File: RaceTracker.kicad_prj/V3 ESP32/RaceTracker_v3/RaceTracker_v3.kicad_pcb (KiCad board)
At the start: 2 copper layers, 50 x 73 mm, 39 parts, among them J1 USB-C, J2 Battery, J3 Qwiic GPS (I2C), J4 microSD, J5 UART Debug, SW1 PWR, SW2 RESET, SW3 BOOT, U1 ESP32-S3-WROOM-1-N8, U2 MCP73831T-2ACI/OT, U3 AP2112K-3.3

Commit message: V3: Wuerth WSEN-ISDS (2536030320001) 6-Achsen-IMU ergaenzt
Beschaltung exakt nach Datenblatt (Rev 001.005, 2025-10-30):
- VDD + VDD_IO an +3V3, je 100nF Entkopplung (C11/C12) -- Standard-
  Bypass-Praxis, da dieses Datenblatt (anders als ESP32/MCP73831/
  AP2112K) keine eigene Beispielschaltung zeigt.
- Pin 2/3 (RSVD) zwingend an VDD_IO (Datenblatt: "Optimize power
  consumption during device start-up sequence").
- Pin 11 (RSVD) an VDD_IO (Datenblatt bietet Wahl: VDD_IO oder NC).
- Pin 10 (RSVD) explizit unverbunden (Datenblatt: "Leave electrically
  unconnected and solder to the PCB").
- CS an VDD_IO (aktiviert I2C-Modus statt SPI).
- SAO ueber R15 (10k) nach GND (I2C-Adresse) -- Pull-Widerstand statt
  Direktverbindung, passend zum Board-Konvention (R1-R14 sind alle
  Pull-Widerstaende) und vermeidet eine ERC-Warnung (Bidirectional-Pin
  direkt an denselben Netz-Knoten wie der GND-PWR_FLAG).
- SCL/SDA an den bestehenden I2C-Bus (teilt sich mit dem externen
  GPS-Modul an J3).
- INT_0/INT_1 offen (optionale Wake/Data-Ready-Ausgaenge, fuer reines
  I2C-Polling nicht noetig) -- explizite No-Connect-Marker.

Kein offizielles KiCad-Symbol fuer dieses Bauteil vorhanden -- eigenes
14-Pin-Symbol gezeichnet, echtes Footprint "Package_LGA:LGA-14_3x2.5mm_
P0.5mm_LayoutBorder3x4y" (urspruenglich fuer ST LSM6DS3 erstellt --
identisches LGA-14/0.5mm-Pitch/3-4-3-4-Pinout-Package, Land-Pattern-Maße
im WSEN-ISDS-Datenblatt gegengeprueft). Neue projektlokale Symbolbib-
liothek RaceTracker_v3.kicad_sym + sym-lib-table angelegt (vermeidet
die lib_symbol_issues-Warnung).

Platine von 50x73mm auf 50x85mm vergroessert (war bereits komplett
vollgepackt, kein Platz fuer 4 neue Bauteile) -- neue Reihe U4/R15/C11/
C12 unten platziert, bestehende Platzierung unangetastet. Default-
Clearance von 0.2mm auf 0.127mm gelockert (die LGA-14-eigenen Pads
liegen bauartbedingt bei 0.5mm Pitch teils nur 0.15-0.175mm auseinander
-- selbe Art Fix wie zuvor bei den ESP32-EPAD-Vias).

ERC: 0 Fehler, 0 Warn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
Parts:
- added C11: 100nF, C_0603_1608Metric, F.Cu at (28.0, 79.0)
- added C12: 100nF, C_0603_1608Metric, F.Cu at (36.0, 79.0)
- added R15: 10k, R_0603_1608Metric, F.Cu at (20.0, 79.0)
- added U4: WSEN-ISDS, LGA-14_3x2.5mm_P0.5mm_LayoutBorder3x4y, F.Cu at (10.0, 79.0)
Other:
- board size 50 x 73 mm -> 50 x 85 mm

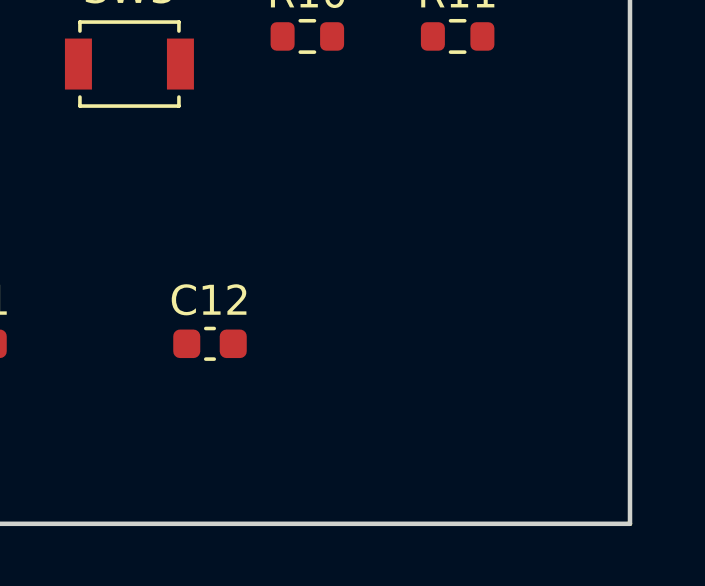
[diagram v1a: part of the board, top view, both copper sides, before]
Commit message: V3: PCB auf 4 Lagen (JLCPCB-Standard-Stackup) + C13 (10uF) fuer WSEN-ISDS
Layer-Stackup 2 -> 4 Lagen (In1.Cu/In2.Cu ergaenzt), physischer Aufbau
exakt nach JLCPCB-Standard-4-Lagen-1.6mm-Build (JLC7628-Klasse):
F.Cu 1oz / Prepreg 7628 0.2104mm / In1.Cu 0.5oz / Core FR4 1.065mm /
In2.Cu 0.5oz / Prepreg 7628 0.2104mm / B.Cu 1oz -- angelegt fuer GND-
und VCC-Plane auf den Innenlagen (Zonen/Pours folgen beim eigentlichen
Routing).

C13 (10uF, 0805) ergaenzt: erneute Pruefung von Wuerths eigenem
"Application circuit" (User Manual Figur 3, Seite 17) zeigte, dass VDD
zusaetzlich zum 100nF (C11) auch einen 10uF-Bulk-Kondensator parallel
braucht ("highly recommended") -- war in der ersten Bestueckung uebersehen
worden. VDD_IO (C12, nur 100nF) stimmte bereits exakt mit der Abbildung
ueberein. User-Manual als Referenz mit im Projekt abgelegt.

ERC: 0/0. DRC: 0 Violations, 122 unverbundene Punkte (weiterhin
ungeroutet, erwartet).

Co-Authored-By: Claude Sonnet 5 <noreply@anthropic.com>
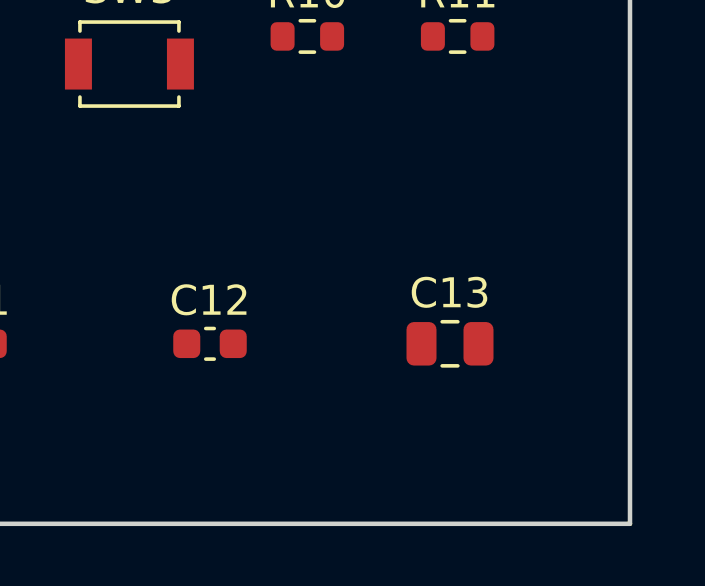
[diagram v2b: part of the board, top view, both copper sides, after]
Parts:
- added C13: 10uF, C_0805_2012Metric, F.Cu at (44.0, 79.0)
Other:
- copper layers 2 -> 4
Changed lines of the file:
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@@
 	(layers
 		(0 "F.Cu" signal)
+		(4 "In1.Cu" signal)
+		(6 "In2.Cu" signal)
 		(2 "B.Cu" signal)
 		(9 "F.Adhes" user "F.Adhesive")
@@
 	)
 	(setup
+		(stackup
+			(layer "F.SilkS"
+				(type "Top Silk Screen")
+			)
+			(layer "F.Paste"
+				(type "Top Solder Paste")
+			)
+			(layer "F.Mask"
+				(type "Top Solder Mask")
+				(thickness 0.01)
+			)
+			(layer "F.Cu"
+				(type "copper")
+				(thickness 0.035)
+			)
+			(layer "dielectric 1"
+				(type "prepreg")
+				(thickness 0.2104)
+				(material "PP 7628")
+				(epsilon_r 4.5)
+				(loss_tangent 0.02)
+			)
+			(layer "In1.Cu"
+				(type "copper")
+				(thickness 0.0175)
+			)
+			(layer "dielectric 2"
+				(type "core")
+				(thickness 1.065)
+				(material "FR4")
+				(epsilon_r 4.5)
+				(loss_tangent 0.02)
+			)
+			(layer "In2.Cu"
+				(type "copper")
+				(thickness 0.0175)
+			)
+			(layer "dielectric 3"
+				(type "prepreg")
+				(thickness 0.2104)
+				(material "PP 7628")
+				(epsilon_r 4.5)
+				(loss_tangent 0.02)
+			)
+			(layer "B.Cu"
+				(type "copper")
+				(thickness 0.035)
+			)
+			(layer "B.Mask"
+				(type "Bottom Solder Mask")
+				(thickness 0.01)
+			)
+			(layer "B.Paste"
+				(type "Bottom Solder Paste")
+			)
+			(layer "B.SilkS"
+				(type "Bottom Silk Screen")
+			)
+			(copper_finish "None")
+			(dielectric_constraints no)
+		)
 		(pad_to_mask_clearance 0)
 		(allow_soldermask_bridges_in_footprints no)
@@
 			(offset
 				(xyz 0 0 0)
+			)
+			(scale
+				(xyz 1 1 1)
+			)
+			(rotate
+				(xyz 0 0 0)
+			)
+		)
+	)
+	(footprint "C_0805_2012Metric"
+		(layer "F.Cu")
+		(at 44 79)
+		(descr "Capacitor SMD 0805 (2012 Metric), square (rectangular) end terminal, IPC-7351 nominal, (Body size source: IPC-SM-782 page 76, https://www.pcb-3d.com/wordpress/wp-content/uploads/ipc-sm-782a_amendment_1_and_2.pdf, https://docs.google.com/spreadsheets/d/1BsfQQcO9C6DZCsRaXUlFlo91Tg2WpOkGARC1WS5S8t0/edit?usp=sharing)")
+		(tags "capacitor")
+		(property "Reference" "C13"
+			(at 0 -1.68 0)
+			(layer "F.SilkS")
+			(effects
+				(font
+					(size 1 1)
+					(thickness 0.15)
+				)
+			)
+		)
+		(property "Value" "10uF"
+			(at 0 1.68 0)
+			(layer "F.Fab")
+			(effects
+				(font
+					(size 1 1)
+					(thickness 0.15)
+				)
+			)
+		)
+		(property "Datasheet" ""
+			(at 0 0 0)
+			(layer "F.Fab")
+			(hide yes)
+			(effects
+				(font
+					(size 1.27 1.27)
+				)
+			)
+		)
+		(property "Description" ""
+			(at 0 0 0)
+			(layer "F.Fab")
+			(hide yes)
+			(effects
+				(font
+					(size 1.27 1.27)
+				)
+			)
+		)
+		(property "KiLib_Generator" "SMD_2terminal_chip_molded"
+			(at 0 0 0)
+			(layer "F.SilkS")
+			(hide yes)
+			(effects
+				(font
+					(size 1 1)
+					(thickness 0.15)
+				)
+			)
+		)
+		(attr smd)
+		(duplicate_pad_numbers_are_jumpers no)
+		(fp_line
+			(start -0.261252 -0.735)
+			(end 0.261252 -0.735)
+			(stroke
+				(width 0.12)
+				(type solid)
+			)
+			(layer "F.SilkS")
+		)
+		(fp_line
+			(start -0.261252 0.735)
+			(end 0.261252 0.735)
+			(stroke
+				(width 0.12)
+				(type solid)
+			)
+			(layer "F.SilkS")
+		)
+		(fp_rect
+			(start -1.7 -0.98)
+			(end 1.7 0.98)
+			(stroke
+				(width 0.05)
+				(type solid)
+			)
+			(fill no)
+			(layer "F.CrtYd")
+		)
+		(fp_rect
+			(start -1 -0.625)
+			(end 1 0.625)
+			(stroke
+				(width 0.1)
+				(type solid)
+			)
+			(fill no)
+			(layer "F.Fab")
+		)
+		(fp_text user "${REFERENCE}"
+			(at 0 0 0)
+			(layer "F.Fab")
+			(effects
+				(font
+					(size 0.5 0.5)
+					(thickness 0.08)
+				)
+			)
+		)
+		(pad "1" smd roundrect
+			(at -0.95 0)
+			(size 1 1.45)
+			(layers "F.Cu" "F.Mask" "F.Paste")
+			(roundrect_rratio 0.25)
+			(net "/+3V3")
+		)
+		(pad "2" smd roundrect
+			(at 0.95 0)
+			(size 1 1.45)
+			(layers "F.Cu" "F.Mask" "F.Paste")
+			(roundrect_rratio 0.25)
+			(net "/GND")
+		)
+		(embedded_fonts no)
+		(model "${KICAD10_3DMODEL_DIR}/Capacitor_SMD.3dshapes/C_0805_2012Metric.step"
+			(offset
+				(xyz 0 0 0)

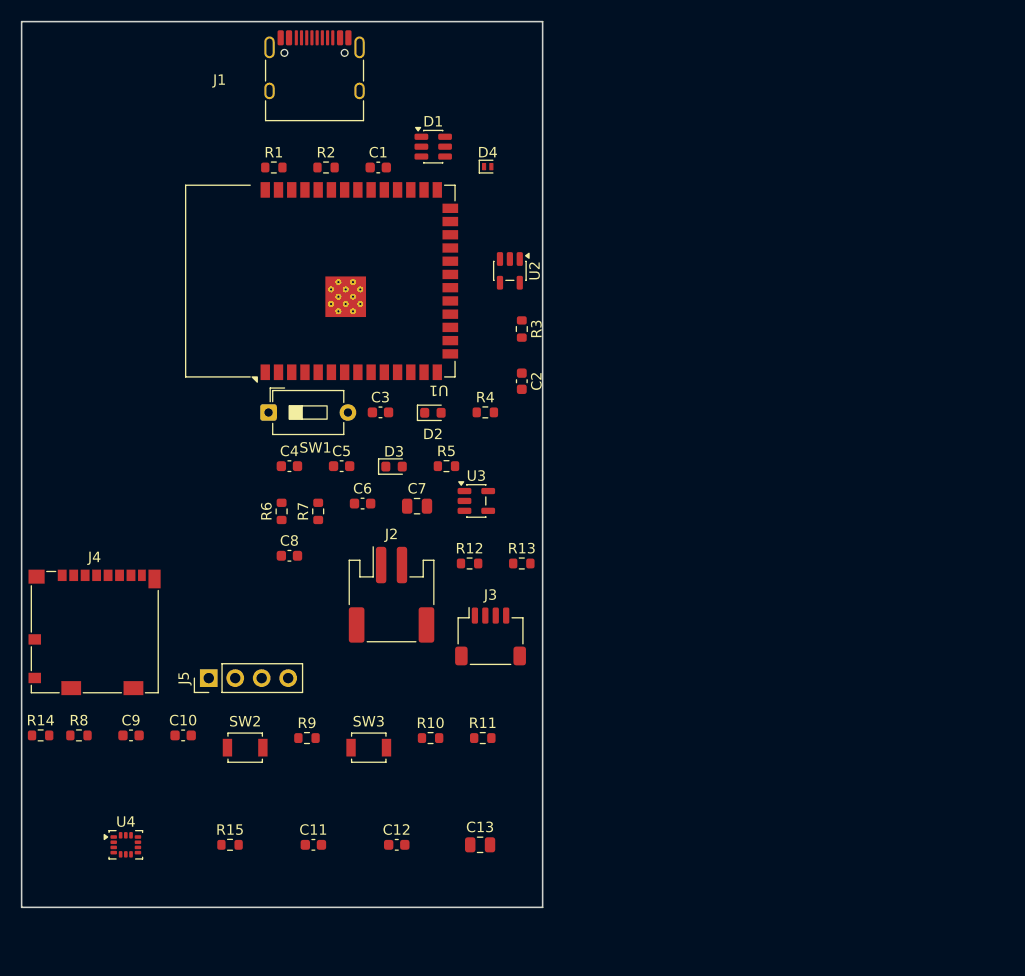
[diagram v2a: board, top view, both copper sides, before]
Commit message: V3: Board auf 50x87mm vergroessert, J6 am Rand platziert
Co-Authored-By: Claude Sonnet 5 <noreply@anthropic.com>
Claude-Session: https://claude.ai/code/session_01KJ1x8W8LsYuDo52VfB14br
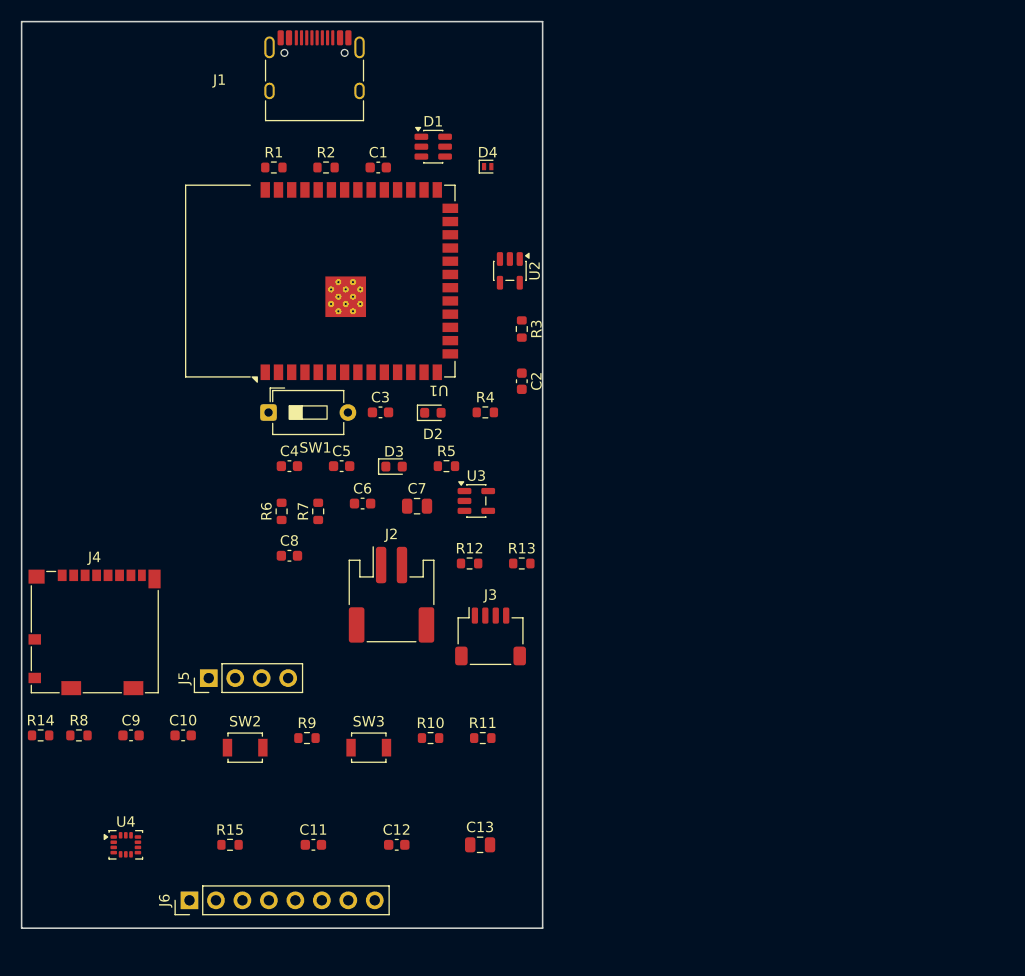
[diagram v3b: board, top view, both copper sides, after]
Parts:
- added J6: e-Paper (steckbar) 8p, PinHeader_1x08_P2.54mm_Vertical, F.Cu at (16.1, 84.3)
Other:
- board size 50 x 85 mm -> 50 x 87 mm

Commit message: V3: GND/+3V3 Planes, Power-Routing, Teilrouting der Signalnetze
Co-Authored-By: Claude Sonnet 5 <noreply@anthropic.com>
Claude-Session: https://claude.ai/code/session_01KJ1x8W8LsYuDo52VfB14br
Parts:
- moved U4 86.9 mm to (82.5, 31.0)
- moved J4 79.7 mm to (83.0, 82.5), turned to 90 degrees
- moved R15 76.6 mm to (79.0, 30.2), turned to 180 degrees
- moved R14 75.4 mm to (74.5, 88.5)
- moved C11 74.3 mm to (86.0, 32.5)
- moved R9 65.3 mm to (88.0, 44.5), turned to 180 degrees
- moved C12 65.0 mm to (82.5, 33.7)
- moved C13 64.5 mm to (86.5, 30.5)
- moved C9 63.6 mm to (74.0, 65.0), turned to 90 degrees
- moved R8 62.5 mm to (68.0, 68.5), turned to 90 degrees
- moved SW3 59.0 mm to (85.0, 41.2), turned to -90 degrees
- moved C4 58.7 mm to (76.0, 73.0)
- moved C10 56.6 mm to (72.0, 65.0), turned to 90 degrees
- moved C5 55.4 mm to (76.0, 74.5)
- moved SW1 53.9 mm to (56.2, 80.5)
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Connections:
- R1 pad 1: Net-(J1-CC1) -> /GND
- R1 pad 2: /GND -> Net-(J1-CC1)
- R2 pad 1: Net-(J1-CC2) -> /GND
- R2 pad 2: /GND -> Net-(J1-CC2)
- U1 pad 4: (no net) -> /EPD_CS
- U1 pad 5: (no net) -> /EPD_DC
- U1 pad 6: (no net) -> /EPD_RST
- U1 pad 7: (no net) -> /EPD_BUSY
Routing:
- net /+VBUS: track 0.00 -> 55.7 mm, vias 0 -> 7
- net /SD_CD: track 0.00 -> 51.6 mm, vias 0 -> 3
- net /+VBAT_RAW: track 0.00 -> 39.0 mm, vias 0 -> 1
- net /SD_CS: track 0.00 -> 37.6 mm, vias 0 -> 2
- net /GND: track 0.00 -> 28.6 mm, vias 0 -> 41
- net /+VBAT_SYS: track 0.00 -> 23.5 mm, vias 0 -> 3
- net /USB_DP: track 0.00 -> 22.4 mm, vias 0 -> 2
- net /SD_MOSI: track 0.00 -> 20.0 mm
- net /USB_DM: track 0.00 -> 18.6 mm
- net /SD_SCK: track 0.00 -> 16.8 mm, vias 0 -> 1
- net /+3V3: track 0.00 -> 15.3 mm, vias 0 -> 22
- net Net-(U1-EN): track 0.00 -> 12.6 mm, vias 0 -> 2
- net Net-(U1-IO0): track 0.00 -> 4.80 mm
- net /BATT_SENSE: track 0.00 -> 4.25 mm
- net /I2C_SDA: track 0.00 -> 3.12 mm
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- added copper zone on In2.Cu, net /+3V3
- added copper zone on In1.Cu, net /GND
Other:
- board size 50 x 87 mm -> 46 x 61 mm

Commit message: V3: Routing zurueckgesetzt (nur Platzierung), fuer Neu-Platzierung
Co-Authored-By: Claude Sonnet 5 <noreply@anthropic.com>
Claude-Session: https://claude.ai/code/session_01KJ1x8W8LsYuDo52VfB14br
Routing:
- net /+VBUS: track 55.7 -> 0.00 mm, vias 7 -> 0
- net /SD_CD: track 51.6 -> 0.00 mm, vias 3 -> 0
- net /+VBAT_RAW: track 39.0 -> 0.00 mm, vias 1 -> 0
- net /SD_CS: track 37.6 -> 0.00 mm, vias 2 -> 0
- net /GND: track 28.6 -> 0.00 mm, vias 41 -> 0
- net /+VBAT_SYS: track 23.5 -> 0.00 mm, vias 3 -> 0
- net /USB_DP: track 22.4 -> 0.00 mm, vias 2 -> 0
- net /SD_MOSI: track 20.0 -> 0.00 mm
- net /USB_DM: track 18.6 -> 0.00 mm
- net /SD_SCK: track 16.8 -> 0.00 mm, vias 1 -> 0
- net /+3V3: track 15.3 -> 0.00 mm, vias 22 -> 0
- net Net-(U1-EN): track 12.6 -> 0.00 mm, vias 2 -> 0
- net Net-(U1-IO0): track 4.80 -> 0.00 mm
- net /BATT_SENSE: track 4.25 -> 0.00 mm
- net /I2C_SDA: track 3.12 -> 0.00 mm
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- removed copper zone on In2.Cu, net /+3V3
- removed copper zone on In1.Cu, net /GND

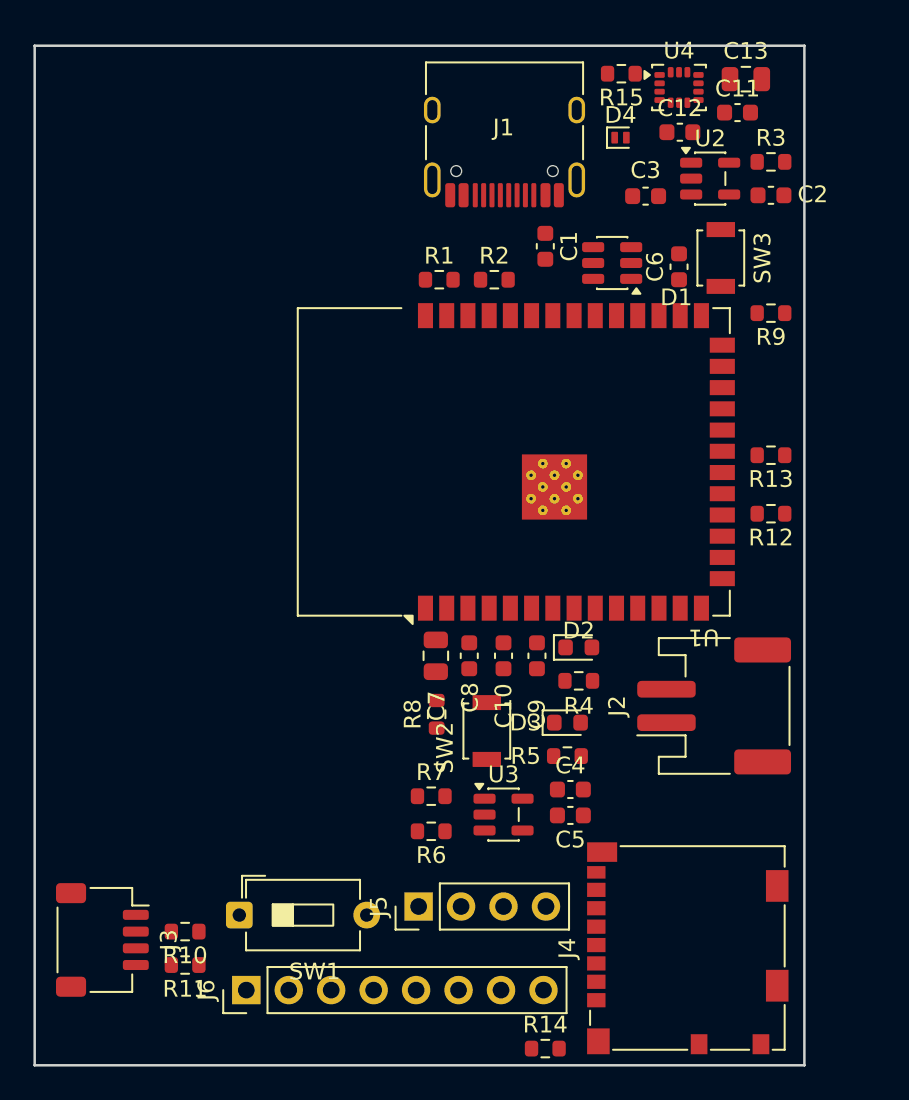
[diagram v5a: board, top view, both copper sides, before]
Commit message: V3: R/C (ausser kritische HF-Entkopplung) auf Rueckseite geflippt
Co-Authored-By: Claude Sonnet 5 <noreply@anthropic.com>
Claude-Session: https://claude.ai/code/session_01KJ1x8W8LsYuDo52VfB14br
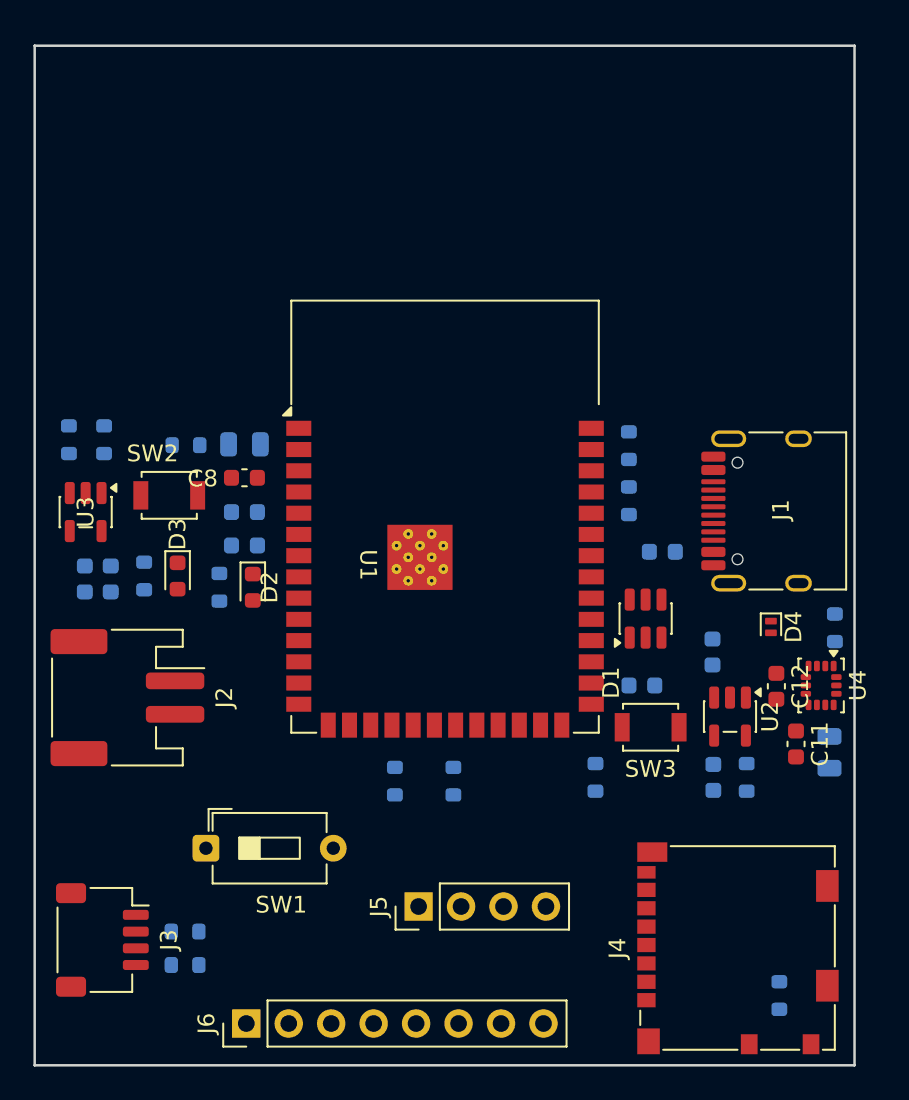
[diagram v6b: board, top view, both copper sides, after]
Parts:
- C1, C10, C13, C2, C3, C4, C5, C6, C7, C9, R1, R10, R11, R12, R13, R14, R15, R2, R3, R4, R5, R6, R7, R8, R9: moved to B.Cu
- moved C13 40.6 mm to (91.5, 70.8), turned to -90 degrees
- moved C11 37.9 mm to (89.5, 70.3), turned to -90 degrees
- moved R3 36.9 mm to (86.5, 72.3), turned to -90 degrees
- moved U4 36.8 mm to (91.0, 66.8), turned to -90 degrees
- moved R15 35.5 mm to (91.8, 63.3), turned to 90 degrees
- moved J2 35.1 mm to (49.5, 67.5), turned to -90 degrees
- moved C2 35.0 mm to (84.5, 72.3), turned to -90 degrees
- moved C12 33.6 mm to (88.3, 66.8), turned to -90 degrees
- moved C5 32.3 mm to (47.0, 60.4), turned to -90 degrees
- moved U2 32.2 mm to (85.5, 68.6), turned to -90 degrees
- moved R6 31.9 mm to (46.0, 52.1), turned to 90 degrees
- moved U3 30.9 mm to (47.0, 56.4), turned to -90 degrees
- moved D4 30.6 mm to (88.0, 63.3), turned to -90 degrees
- moved C4 30.2 mm to (48.5, 60.4), turned to -90 degrees
- moved R9 29.7 mm to (77.5, 72.3), turned to 90 degrees
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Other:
- board size 46 x 61 mm -> 49 x 61 mm
